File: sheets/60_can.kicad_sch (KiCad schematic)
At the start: 2 parts, among them U1 ADM3055E

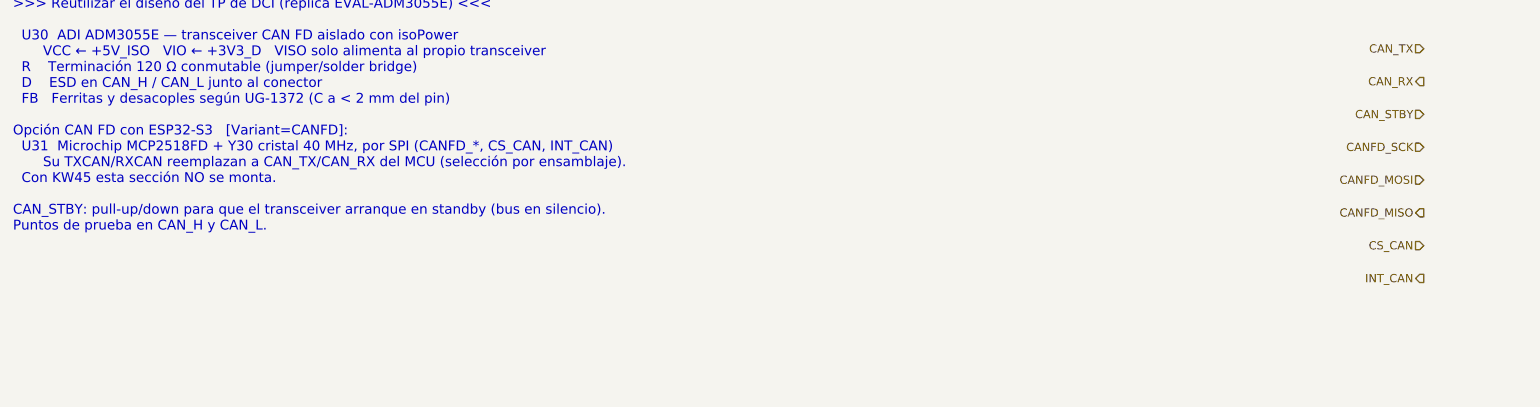
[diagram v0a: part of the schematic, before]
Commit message: Alcance: solo ESP32-S3, CAN clásico por TWAI, sin MCP2518FD
- Raíz: el bloque 40_mcu apunta a 40_mcu_esp32s3. 40_mcu_kw45 queda en
  el repo solo como referencia, fuera de la jerarquía.
- CAN: se eliminan el MCP2518FD, el cristal y los pines CANFD_SCK/MOSI/
  MISO, CS_CAN e INT_CAN en 60_can, 40_mcu_esp32s3 y la raíz (etiquetas,
  cables y pines de hoja). TWAI nativo (J1939) directo al ADM3055E.
  Se quita la variante CANFD.
- 20_isolation (nota): PS1 >= 5 W y entrada 9-72 V (corte OV 38.4 V);
  U2 = TPS7A1650-Q1 para +5V_VEH.
- 40_mcu_esp32s3 (nota): desacople 22 uF + 100 nF según Espressif y
  límite de 47 uF en +3V3_D por el TPS62A02-Q1; solo BLE en operación.
- README: tabla corregida (LM74930-Q1 en 10_power_input, 20, 30, 40, 60),
  sección MCU y "Requisitos para el firmware" (rearme del latch >= 100 ms,
  arranque limpio tras brownout, NimBLE con WiFi desactivado).
- CLAUDE.md: sección "Alcance" (ESP32-S3 único, dimensionar con WiFi).

ERC: 180 -> 160 violaciones; sin errores nuevos. Las restantes son de
hojas sin terminar (20, 30, 60) y etiquetas de la raíz sin destino.

Co-Authored-By: Claude Opus 5.5 <noreply@anthropic.com>
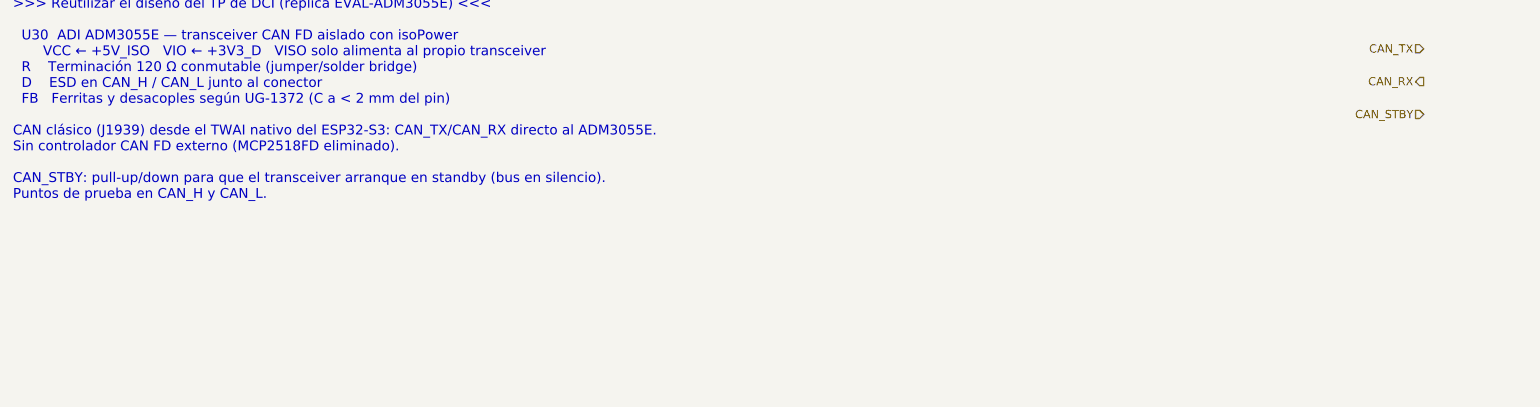
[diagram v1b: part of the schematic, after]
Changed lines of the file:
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@@
 		)
 	)
-	(text "BLOQUE 60 — CAN AISLADO, BARRERA 2  [ISO ║ BUS]   [Variant=CAN]\n>>> Reutilizar el diseño del TP de DCI (réplica EVAL-ADM3055E) <<<\n\n  U30  ADI ADM3055E — transceiver CAN FD aislado con isoPower\n       VCC ← +5V_ISO   VIO ← +3V3_D   VISO solo alimenta al propio transceiver\n  R    Terminación 120 Ω conmutable (jumper/solder bridge)\n  D    ESD en CAN_H / CAN_L junto al conector\n  FB   Ferritas y desacoples según UG-1372 (C a < 2 mm del pin)\n\nOpción CAN FD con ESP32-S3   [Variant=CANFD]:\n  U31  Microchip MCP2518FD + Y30 cristal 40 MHz, por SPI (CANFD_*, CS_CAN, INT_CAN)\n       Su TXCAN/RXCAN reemplazan a CAN_TX/CAN_RX del MCU (selección por ensamblaje).\n  Con KW45 esta sección NO se monta.\n\nCAN_STBY: pull-up/down para que el transceiver arranque en standby (bus en silencio).\nPuntos de prueba en CAN_H y CAN_L."
+	(text "BLOQUE 60 — CAN AISLADO, BARRERA 2  [ISO ║ BUS]   [Variant=CAN]\n>>> Reutilizar el diseño del TP de DCI (réplica EVAL-ADM3055E) <<<\n\n  U30  ADI ADM3055E — transceiver CAN FD aislado con isoPower\n       VCC ← +5V_ISO   VIO ← +3V3_D   VISO solo alimenta al propio transceiver\n  R    Terminación 120 Ω conmutable (jumper/solder bridge)\n  D    ESD en CAN_H / CAN_L junto al conector\n  FB   Ferritas y desacoples según UG-1372 (C a < 2 mm del pin)\n\nCAN clásico (J1939) desde el TWAI nativo del ESP32-S3: CAN_TX/CAN_RX directo al ADM3055E.\nSin controlador CAN FD externo (MCP2518FD eliminado).\n\nCAN_STBY: pull-up/down para que el transceiver arranque en standby (bus en silencio).\nPuntos de prueba en CAN_H y CAN_L."
 		(exclude_from_sim no)
 		(at 20.32 20.32 0)
@@
 		)
 	)
-	(hierarchical_label "CANFD_MOSI"
-		(shape input)
-		(at 238.76 50.8 180)
-		(effects
-			(font
-				(size 1.27 1.27)
-			)
-			(justify right)
-		)
-	)
 	(hierarchical_label "CAN_TX"
 		(shape input)
 		(at 238.76 30.48 180)
-		(effects
-			(font
-				(size 1.27 1.27)
-			)
-			(justify right)
-		)
-	)
-	(hierarchical_label "INT_CAN"
-		(shape output)
-		(at 238.76 66.04 180)
 		(effects
 			(font
@@
 		)
 	)
-	(hierarchical_label "CS_CAN"
-		(shape input)
-		(at 238.76 60.96 180)
-		(effects
-			(font
-				(size 1.27 1.27)
-			)
-			(justify right)
-		)
-	)
 	(hierarchical_label "CAN_SILENT"
 		(shape input)
@@
 		(effects
 			(font
-				(size 1.27 1.27)
-			)
-			(justify right)
-		)
-	)
-	(hierarchical_label "CANFD_MISO"
-		(shape output)
-		(at 238.76 55.88 180)
-		(effects
-			(font
-				(size 1.27 1.27)
-			)
-			(justify right)
-		)
-	)
-	(hierarchical_label "CANFD_SCK"
-		(shape input)
-		(at 238.76 45.72 180)
-		(effects
-			(font

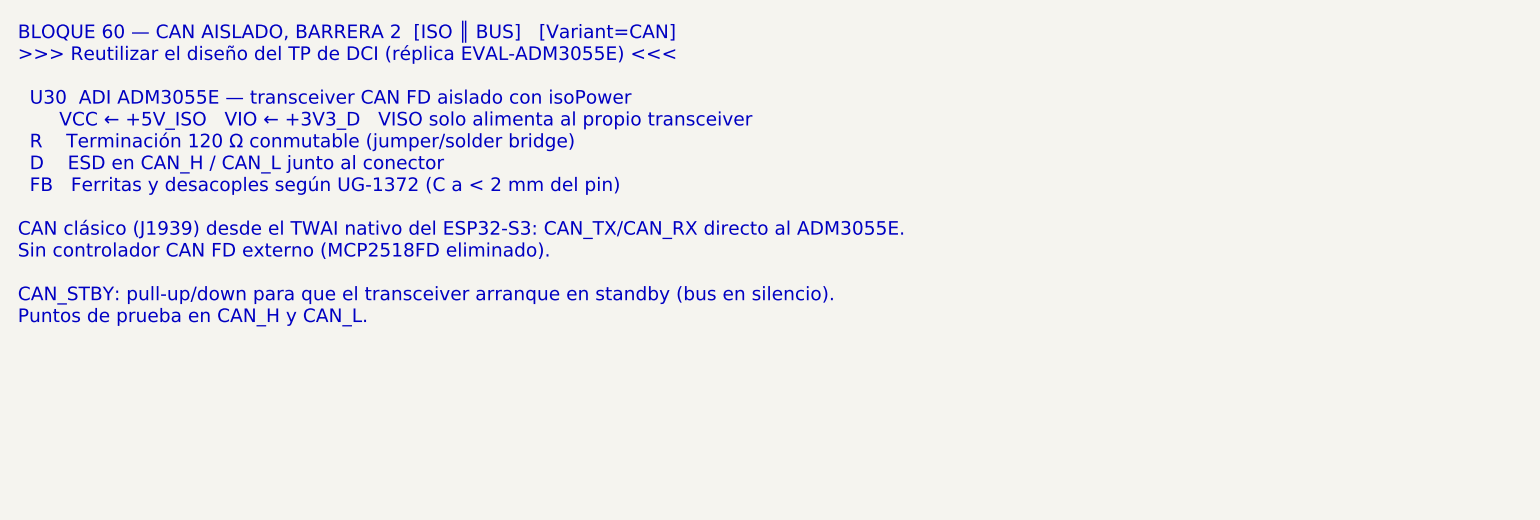
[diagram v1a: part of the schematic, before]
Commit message: ADM3055E: consumo de VCC confirmado con el datasheet Rev. D
- ICC en dominante con RL = 60 ohm: 180 mA típ / 260 mA máx (tabla 1);
  IIO 3.6 / 5 mA. Anotado en 60_can.
- +5V_ISO pico: 0.26 A (ADM3055E) + 0.39 A (buck, 521 mA en +3V3_D con
  WiFi TX) + 0.02 A (LDO) = 3.35 W; x1.5 = 5.0 W. PS1 se mantiene en
  >= 5 W (no hace falta 6 W). Nota de 20_isolation actualizada.
- docs/datasheets/adm3055e-adm3057e.pdf.

Co-Authored-By: Claude Opus 5.5 <noreply@anthropic.com>
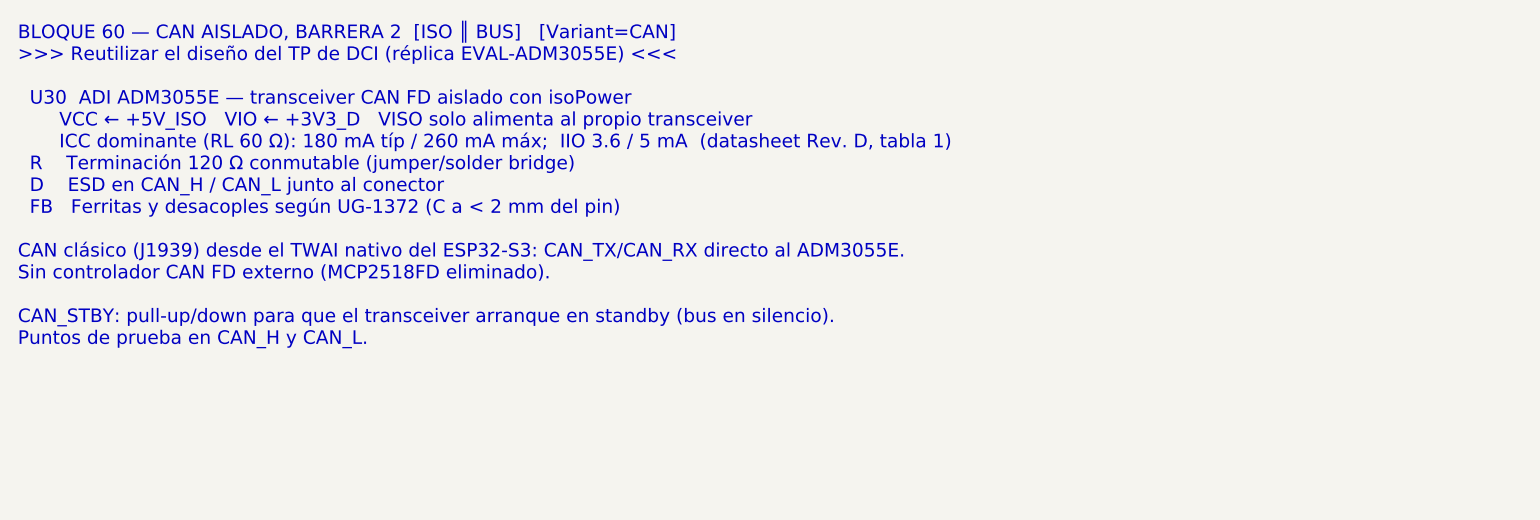
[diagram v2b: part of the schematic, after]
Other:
- note added: "BLOQUE 60 — CAN AISLADO, BARRERA 2 [ISO ║ BUS] [Variant=CAN] >>> Reutilizar el diseño del TP de DCI (réplica EVAL-ADM3055E) <<< U30 ADI ADM3055E — transceiver CAN FD aislado con isoPower VCC ← +5V_ISO VIO ← +3V3_D VISO solo alimenta al propio transceiver ICC dominante (RL 60 Ω): 180 mA típ / 260 mA máx; IIO 3.6 / 5 mA (datasheet Rev. D, tabla 1) R Terminación 120 Ω conmutable (jumper/solder bridg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"
- note removed: "BLOQUE 60 — CAN AISLADO, BARRERA 2 [ISO ║ BUS] [Variant=CAN] >>> Reutilizar el diseño del TP de DCI (réplica EVAL-ADM3055E) <<< U30 ADI ADM3055E — transceiver CAN FD aislado con isoPower VCC ← +5V_ISO VIO ← +3V3_D VISO solo alimenta al propio transceiver R Terminación 120 Ω conmutable (jumper/solder bridge) D ESD en CAN_H / CAN_L junto al conector FB Ferritas y desacoples según UG-1372 (C a < 2 m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"
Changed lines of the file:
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@@
 		)
 	)
-	(text "BLOQUE 60 — CAN AISLADO, BARRERA 2  [ISO ║ BUS]   [Variant=CAN]\n>>> Reutilizar el diseño del TP de DCI (réplica EVAL-ADM3055E) <<<\n\n  U30  ADI ADM3055E — transceiver CAN FD aislado con isoPower\n       VCC ← +5V_ISO   VIO ← +3V3_D   VISO solo alimenta al propio transceiver\n  R    Terminación 120 Ω conmutable (jumper/solder bridge)\n  D    ESD en CAN_H / CAN_L junto al conector\n  FB   Ferritas y desacoples según UG-1372 (C a < 2 mm del pin)\n\nCAN clásico (J1939) desde el TWAI nativo del ESP32-S3: CAN_TX/CAN_RX directo al ADM3055E.\nSin controlador CAN FD externo (MCP2518FD eliminado).\n\nCAN_STBY: pull-up/down para que el transceiver arranque en standby (bus en silencio).\nPuntos de prueba en CAN_H y CAN_L."
+	(text "BLOQUE 60 — CAN AISLADO, BARRERA 2  [ISO ║ BUS]   [Variant=CAN]\n>>> Reutilizar el diseño del TP de DCI (réplica EVAL-ADM3055E) <<<\n\n  U30  ADI ADM3055E — transceiver CAN FD aislado con isoPower\n       VCC ← +5V_ISO   VIO ← +3V3_D   VISO solo alimenta al propio transceiver\n       ICC dominante (RL 60 Ω): 180 mA típ / 260 mA máx;  IIO 3.6 / 5 mA  (datasheet Rev. D, tabla 1)\n  R    Terminación 120 Ω conmutable (jumper/solder bridge)\n  D    ESD en CAN_H / CAN_L junto al conector\n  FB   Ferritas y desacoples según UG-1372 (C a < 2 mm del pin)\n\nCAN clásico (J1939) desde el TWAI nativo del ESP32-S3: CAN_TX/CAN_RX directo al ADM3055E.\nSin controlador CAN FD externo (MCP2518FD eliminado).\n\nCAN_STBY: pull-up/down para que el transceiver arranque en standby (bus en silencio).\nPuntos de prueba en CAN_H y CAN_L."
 		(exclude_from_sim no)
 		(at 20.32 20.32 0)
